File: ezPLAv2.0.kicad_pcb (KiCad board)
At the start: 2 copper layers, 24.5 x 40 mm, 5 parts, among them J1 JTAG-10, J2 Power, J3 PLA-headers, U2 EPM7032

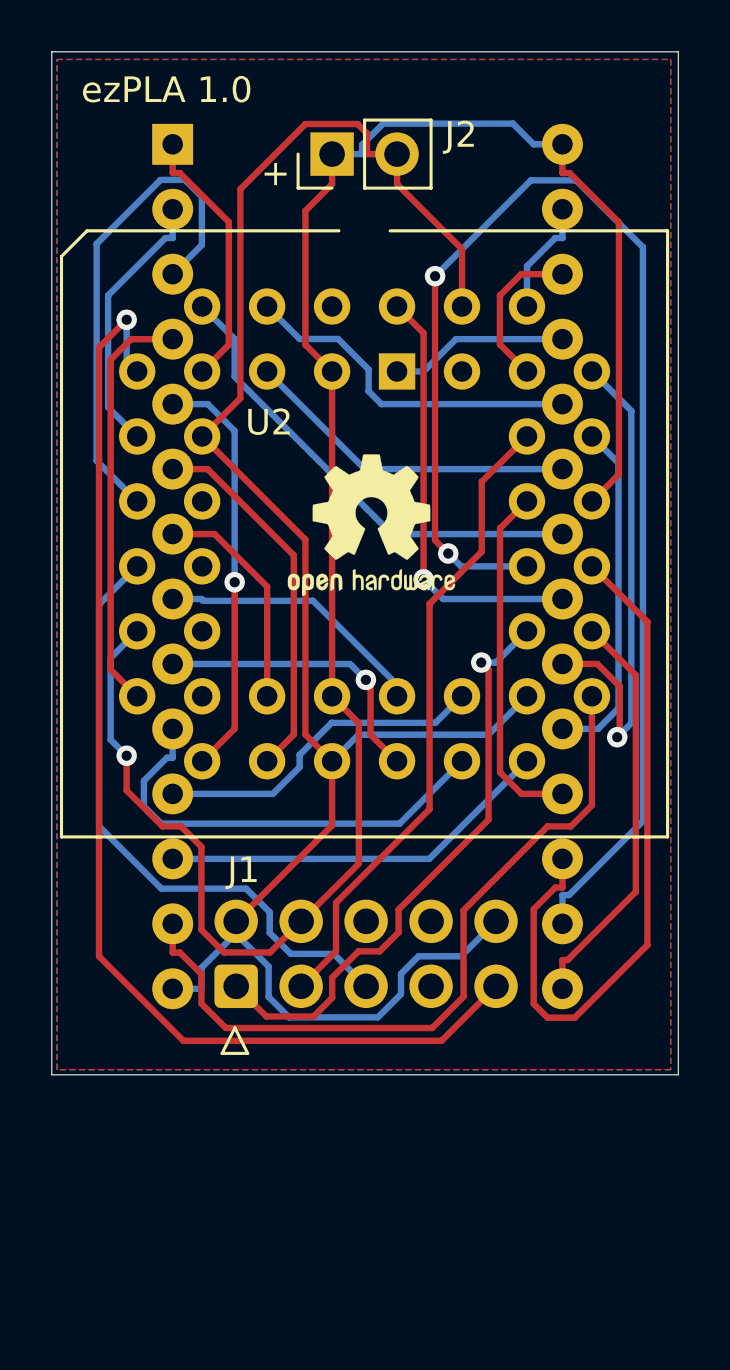
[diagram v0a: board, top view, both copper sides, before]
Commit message: rev2.0 PCB with NAND Gate CASRAM delay
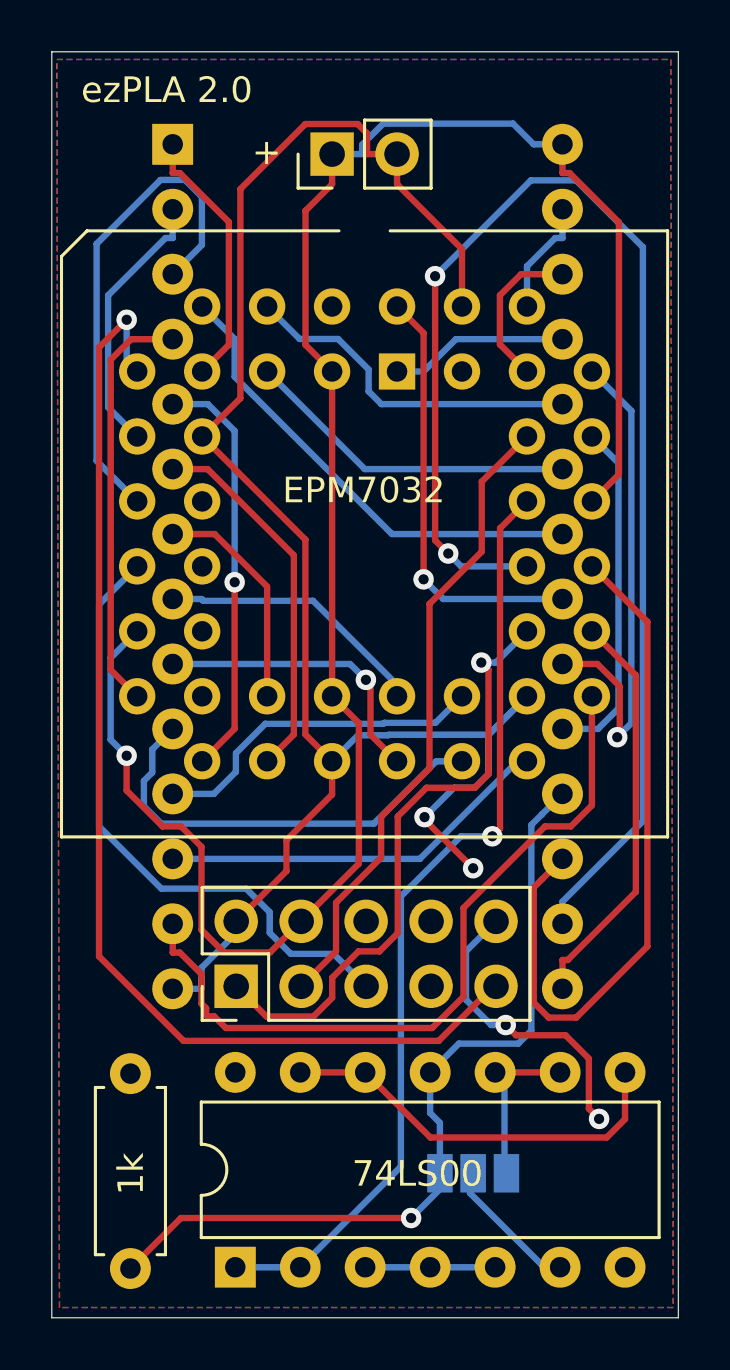
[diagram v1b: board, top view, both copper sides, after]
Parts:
- removed REF**: OSHW-Logo2_7.3x6mm_SilkScreen, Symbol:OSHW-Logo2_7.3x6mm_SilkScreen
- added JP1: Jumper_3_Open, Jumper:SolderJumper-3_P1.3mm_Open_Pad1.0x1.5mm_NumberLabels, B.Cu at (152.0, 142.8)
- added R1: 1k, Resistor_THT:R_Axial_DIN0207_L6.3mm_D2.5mm_P7.62mm_Horizontal, F.Cu at (138.6, 146.6)
- added U1: 74LS00, Package_DIP:DIP-14_W7.62mm, F.Cu at (142.7, 146.5)
- J1: footprint C64_PLA:IDC-Header_2x05_P2.54mm_Custom -> Connector_PinHeader_2.54mm:PinHeader_2x05_P2.54mm_Vertical
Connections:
- J3 pad 18: CASRAM -> CASRAM(d)
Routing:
- net CASRAM(d): track 0.00 -> 32.5 mm, vias 0 -> 1
- net CASRAM: track 13.8 -> 36.9 mm, vias 0 -> 1
- net Net-(U1-Pad12): track 0.00 -> 15.9 mm
- net GND: track 75.3 -> 82.5 mm, vias 0 -> 4
- net Net-(JP1-Pad1): track 0.00 -> 6.60 mm
- net Net-(JP1-Pad2): track 0.00 -> 5.60 mm
- net Net-(U1-Pad3): track 0.00 -> 5.08 mm
- net TCK: track 23.1 -> 24.2 mm
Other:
- board size 24.5 x 40 mm -> 24.5 x 49.5 mm
- board text added: "1k"
- board text added: "74LS00"
- board text added: "EPM7032"
- board text added: "Timing"
- board text added: "ezPLA 2.0"
- board text removed: "ezPLA 1.0"

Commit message: jumpers added
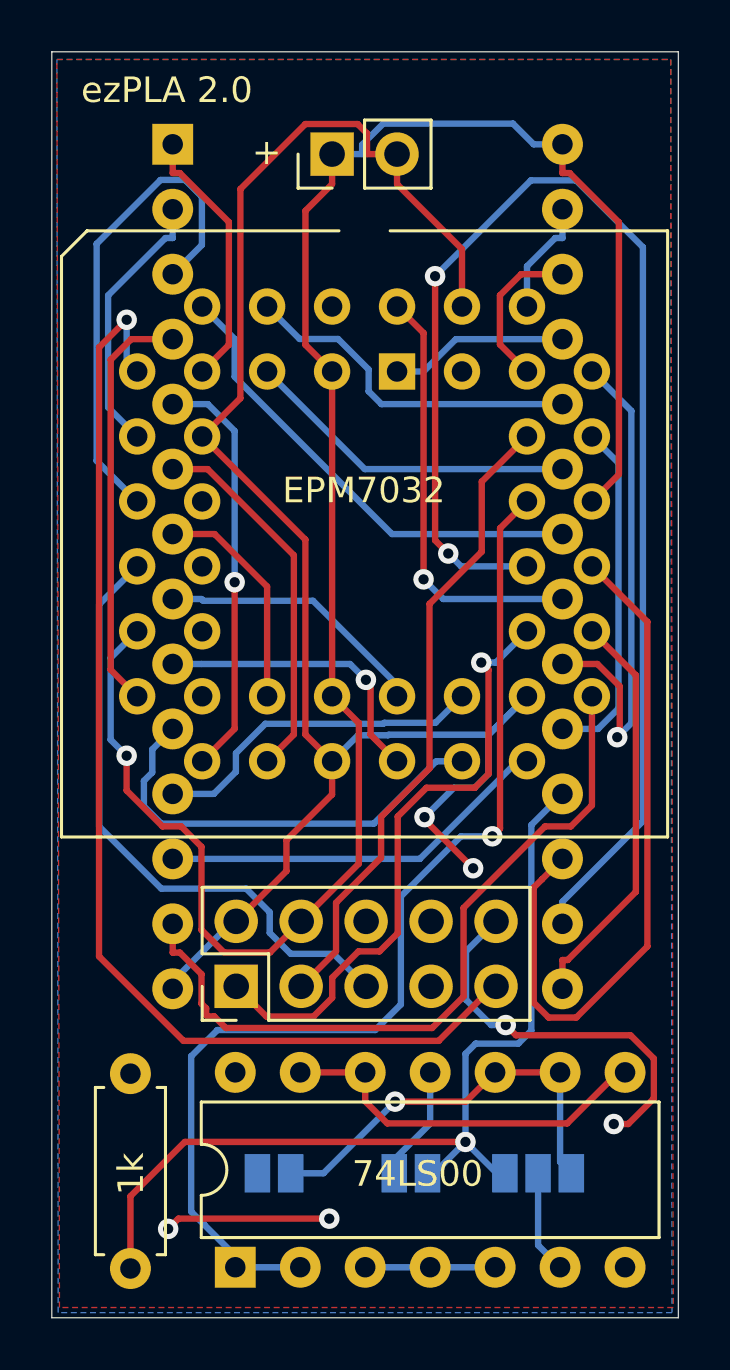
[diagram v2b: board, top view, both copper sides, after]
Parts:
- added JP2: Jumper_2_Open, Jumper:SolderJumper-2_P1.3mm_Open_Pad1.0x1.5mm, B.Cu at (144.2, 142.8)
- added JP3: Jumper_2_Open, Jumper:SolderJumper-2_P1.3mm_Open_Pad1.0x1.5mm, B.Cu at (149.5, 142.8)
- J3: footprint C64_PLA:DIP-28_W15.24mm_mirrored -> ezPLA footprints:DIP-28_W15.24mm_mirrored
- moved JP1 2.54 mm to (154.5, 142.8)
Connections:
- U1 pad 11: CASRAM(d) -> Net-(JP3-Pad2)
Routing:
- net Net-(JP1-Pad1): track 6.60 -> 16.8 mm, vias 0 -> 1
- net GND: track 82.5 -> 92.0 mm, vias 4 -> 6
- net CASRAM: track 36.9 -> 43.0 mm
- net Net-(JP3-Pad2): track 0.00 -> 5.47 mm
- net CASRAM(d): track 32.5 -> 37.3 mm
- net Net-(JP1-Pad2): track 5.60 -> 4.66 mm
- net Net-(U1-Pad12): track 15.9 -> 15.0 mm
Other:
- board text added: "2 Gate"
- board text added: "4 Gate"
